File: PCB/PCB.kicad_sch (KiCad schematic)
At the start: 7 parts, among them J1 Lidar_1, J2 Lidar_2, J3 Lidar_3, J6 Buzzer, U1 Teensy4.0

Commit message: add pullups and second IMU
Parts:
- added J4: IMU_2, Connector_PinHeader_2.54mm:PinHeader_1x04_P2.54mm_Vertical, symbol Connector:Conn_01x04_Socket
- added R1, R2, R3, R4, R5, R6: 4.7k, Resistor_THT:R_Axial_DIN0207_L6.3mm_D2.5mm_P10.16mm_Horizontal, symbol Device:R
- J6: footprint Customs:Buzzer -> Customs:Small_Buzzer
- U1: footprint teensy.pretty-master:Teensy40 -> teensy:Teensy40
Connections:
- net +3V3: now also J4.1 (Pin_1), R1.1, R2.1, R3.1, R4.1, R5.1, R6.1
- net GND: now also MPU6050_Module1.7 (ADO), J4.4 (Pin_4)
- net at J1.2 (Pin_2), MPU6050_Module1.3 (SCL), U1.26 (19_A5_SCL0): now also R4.2
- net at J1.3 (Pin_3), MPU6050_Module1.4 (SDA), U1.25 (18_A4_SDA0): now also R3.2
- net at J2.2 (Pin_2), U1.23 (16_A2_RX4_SCL1): now also J4.2 (Pin_2), R1.2
- net at J2.3 (Pin_3), U1.24 (17_A3_TX4_SDA1): now also J4.3 (Pin_3), R2.2
- net at J3.2 (Pin_2), U1.35 (24_A10_TX6_SCL2): now also R6.2
- net at J3.3 (Pin_3), U1.36 (25_A11_RX6_SDA2): now also R5.2
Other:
- moved on the sheet: J1, J2

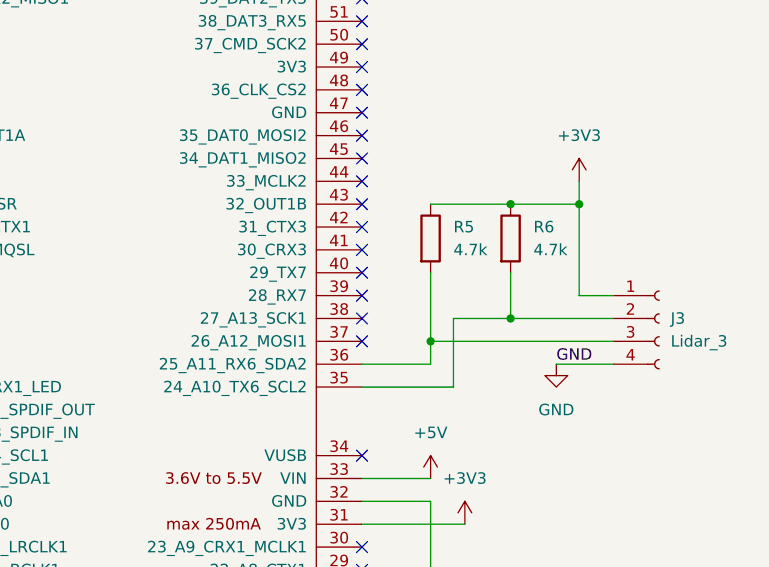
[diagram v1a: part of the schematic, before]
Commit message: mounting holes + vias, extra route for last I2C port
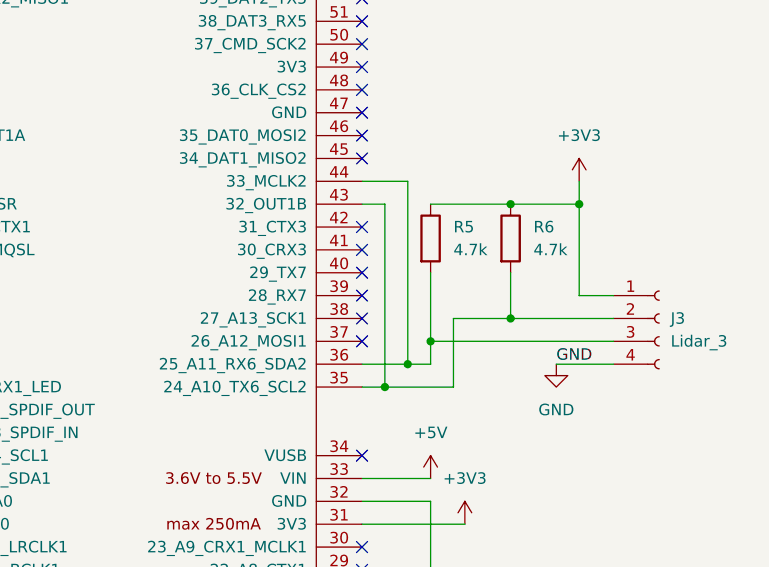
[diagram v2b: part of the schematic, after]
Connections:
- net at J3.2 (Pin_2), R6.2, U1.35 (24_A10_TX6_SCL2): now also U1.43 (32_OUT1B)
- net at J3.3 (Pin_3), R5.2, U1.36 (25_A11_RX6_SDA2): now also U1.44 (33_MCLK2)
- no-connect marks 41 -> 39
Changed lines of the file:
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@@
+	)
+	(junction
+		(at 173.99 91.44)
+		(diameter 0)
+		(color 0 0 0 0)
 	)
 	(junction
@@
 	)
 	(junction
+		(at 176.53 88.9)
+		(diameter 0)
+		(color 0 0 0 0)
+	)
+	(junction
 		(at 187.96 71.12)
 		(diameter 0)
@@
 	)
 	(no_connect
-		(at 171.45 71.12)
-	)
-	(no_connect
 		(at 115.57 111.76)
 	)
 	(no_connect
-		(at 171.45 68.58)
-	)
-	(no_connect
 		(at 115.57 68.58)
 	)
@@
 	(wire
 		(pts
+			(xy 173.99 91.44) (xy 171.45 91.44)
+		)
+		(stroke
+			(width 0)
+			(type default)
+		)
+	)
+	(wire
+		(pts
 			(xy 106.68 45.72) (xy 115.57 45.72)
 		)
@@
 	(wire
 		(pts
-			(xy 181.61 91.44) (xy 171.45 91.44)
+			(xy 173.99 71.12) (xy 173.99 91.44)
+		)
+		(stroke
+			(width 0)
+			(type default)
+		)
+	)
+	(wire
+		(pts
+			(xy 181.61 91.44) (xy 173.99 91.44)
+		)
+		(stroke
+			(width 0)
+			(type default)
+		)
+	)
+	(wire
+		(pts
+			(xy 171.45 68.58) (xy 176.53 68.58)
 		)
 		(stroke
@@
 	(wire
 		(pts
+			(xy 176.53 88.9) (xy 179.07 88.9)
+		)
+		(stroke
+			(width 0)
+			(type default)
+		)
+	)
+	(wire
+		(pts
 			(xy 97.79 167.64) (xy 97.79 172.72)
 		)
@@
 	(wire
 		(pts
-			(xy 171.45 88.9) (xy 179.07 88.9)
+			(xy 171.45 88.9) (xy 176.53 88.9)
 		)
 		(stroke
@@
 	(wire
 		(pts
+			(xy 176.53 68.58) (xy 176.53 88.9)
+		)
+		(stroke
+			(width 0)
+			(type default)
+		)
+	)
+	(wire
+		(pts
 			(xy 87.63 81.28) (xy 87.63 83.82)
 		)
@@
 		)
 		(stroke
+			(width 0)
+			(type default)
+		)
+	)
+	(wire
+		(pts
+			(xy 171.45 71.12) (xy 173.99 71.12)
+		)
+		(stroke
